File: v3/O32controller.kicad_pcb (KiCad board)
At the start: 4 copper layers, 27 x 27 mm, 88 parts, among them J1 SWD, J10 3V3, J11 GND, J12 I2C/RS485_2, J2 BATT+, J3 BATT-, J4 Motor Connection, J5 Motor Connection, J6 Motor Connection, J7 BATT+, J8 BATT-, J9 I2C/RS485_1, Q1 CSD88584Q5DCT, Q2 CSD88584Q5DCT, Q3 CSD88584Q5DCT, SW1 RESET, U1 MA702GQ-P, U2 STSPIN32F0A, U3 THVD1420DRLR

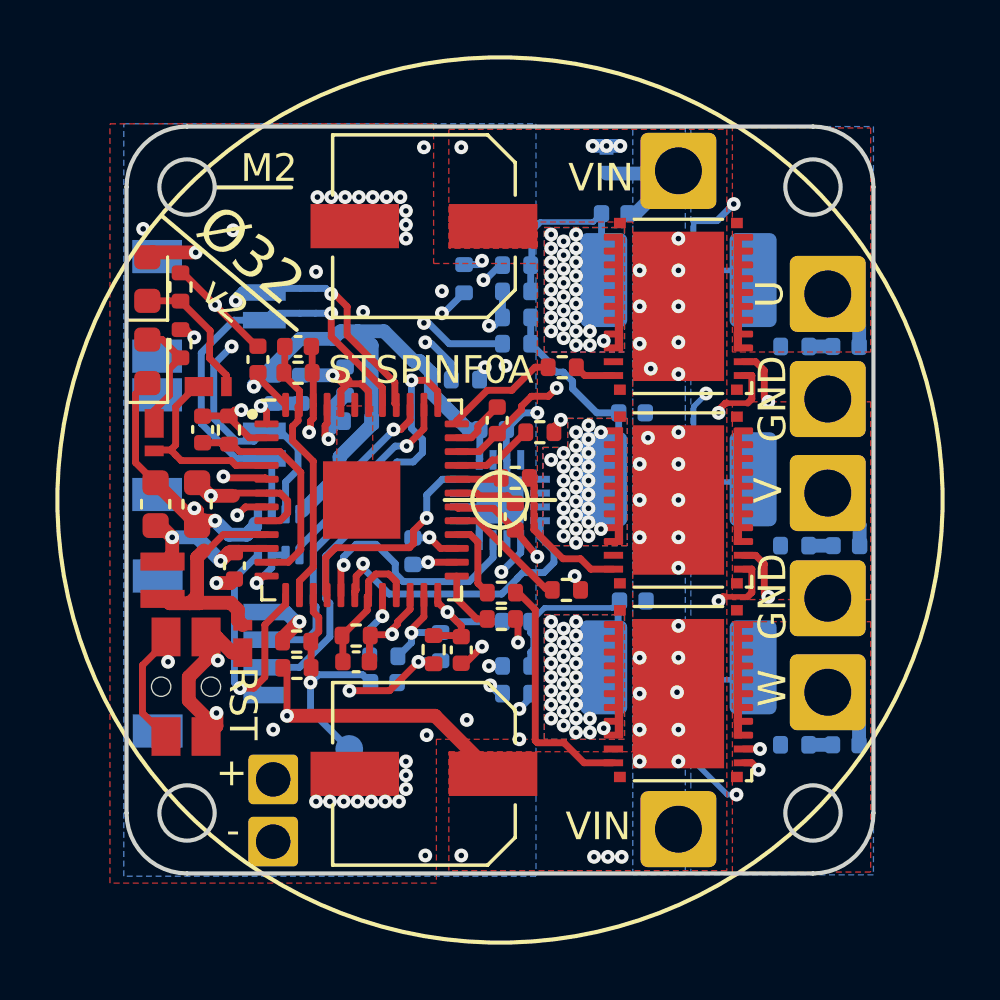
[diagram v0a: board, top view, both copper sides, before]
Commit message: external spi, update bus sns res, routing
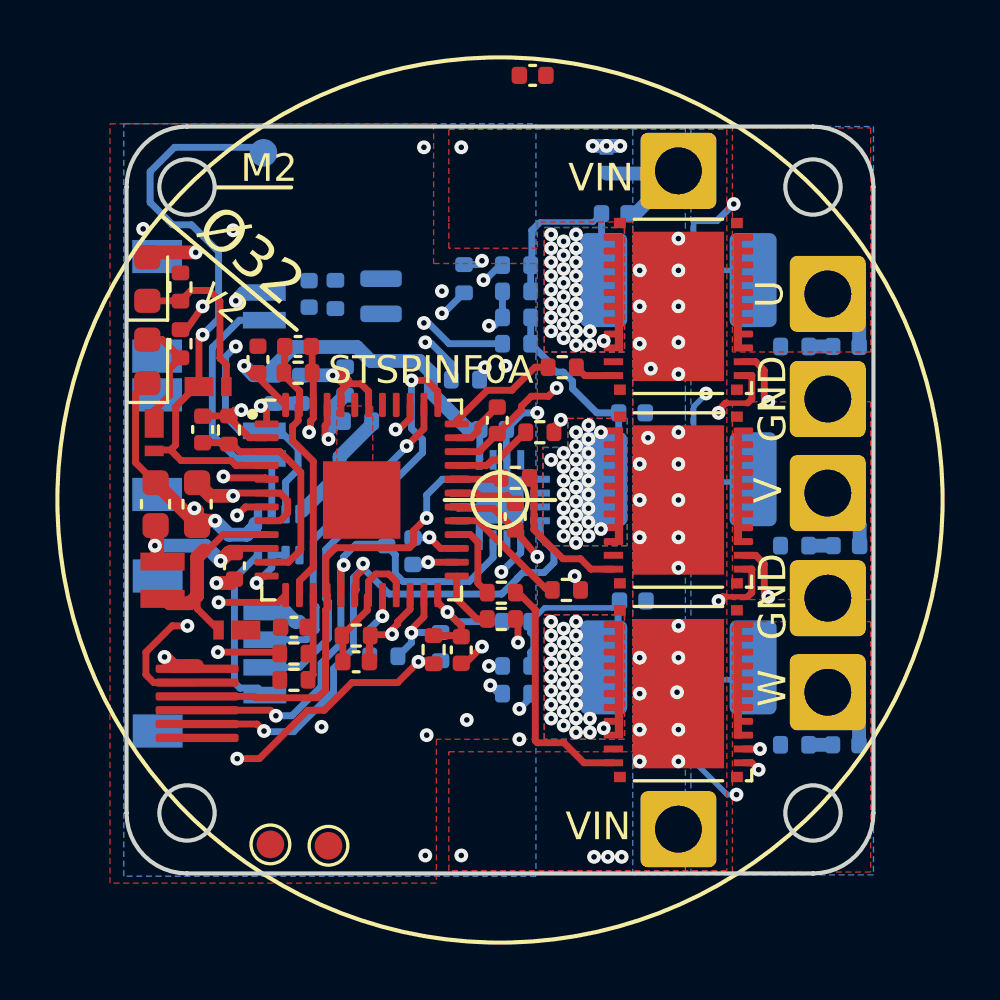
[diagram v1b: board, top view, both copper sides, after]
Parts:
- removed C21: 1nF, Capacitor_SMD:C_0402_1005Metric
- removed J10: 3V3, O32controller:SolderWire-Actual_1x01_D1.25mm_OD_1.8mm
- removed J11: GND, O32controller:SolderWire-Actual_1x01_D1.25mm_OD_1.8mm
- removed NT4: SDA/A, O32controller:NetTie-2_SMD_Pad0.25mm
- removed NT5: SCL/B, O32controller:NetTie-2_SMD_Pad0.25mm
- removed SW1: RESET, O32controller:Tactile_Switch_EVQ-P7A01P
- added C22: 100nF, Capacitor_SMD:C_0402_1005Metric, F.Cu at (42.5, 54.6)
- added J14: NTC, O32controller:SolderNTC-1.27mm, B.Cu at (45.7, 43.3)
- added J15: ExternalSPI, O32controller:FFC_0.5mm_6p, F.Cu at (39.0, 56.1)
- added R36: 1k, Resistor_SMD:R_0402_1005Metric, B.Cu at (44.0, 42.6)
- added R38: 13.7k, Resistor_SMD:R_0402_1005Metric, B.Cu at (45.9, 51.1)
- added TP1: TestPoint, TestPoint:TestPoint_Pad_D1.0mm, F.Cu at (43.8, 62.5)
- added TP2: TestPoint, TestPoint:TestPoint_Pad_D1.0mm, F.Cu at (41.7, 62.5)
- C8: value 100uF -> 20uF; footprint O32controller:CAP_EEEFN1E101UP -> Capacitor_SMD:C_0402_1005Metric
- C9: value 100uF -> 100nF; footprint O32controller:CAP_EEEFN1E101UP -> Capacitor_SMD:C_0402_1005Metric; moved to B.Cu
- J12: value I2C/RS485_2 -> RS485_2
- J9: value I2C/RS485_1 -> RS485_1
- R26: value 41.2k -> 54.9k
- R27: value 10k -> 13.7k
- moved TP3 21.8 mm to (41.5, 37.5)
- moved C9 17.8 mm to (43.1, 42.5), turned to -90 degrees
- moved C8 6.72 mm to (51.2, 34.6)
- moved R27 1.38 mm to (42.5, 56.5), turned to 0 degrees
- moved D1 0.54 mm to (40.5, 54.7), turned to 0 degrees
- moved R26 0.53 mm to (42.5, 55.5)
- renumbered TP2 to TP3
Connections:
- net /~{MAG_CS} renamed /~{MAG1_CS}
- C9 pad 1: VBUS -> /NTC_IN
- R27 pad 1: /BUS_SENSE -> GND
- R27 pad 2: GND -> /BUS_SENSE
- TP3 pad 1: /BUS_SENSE -> /LED_STATUS
- U2 pad 13: USART_TX -> /NTC_IN
- U2 pad 39: /USART_RX -> /~{MAG2_CS}
- U2 pad 40: I2C_SCL -> USART_TX
- U2 pad 41: I2C_SDA -> /USART_RX
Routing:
- net /NTC_IN: track 0.00 -> 22.8 mm, vias 0 -> 1
- net /~{MAG2_CS}: track 0.00 -> 20.3 mm, vias 0 -> 2
- net /LED_STATUS: track 6.93 -> 21.0 mm, vias 0 -> 1
- net GND: track 45.4 -> 33.8 mm, vias 51 -> 24
- net /SPI_MOSI: track 10.9 -> 21.6 mm, vias 1 -> 2
- net /SPI_MISO: track 8.81 -> 18.7 mm, vias 1 -> 2
- net /SPI_SCLK: track 8.16 -> 16.4 mm
- net /USART_RX: track 6.95 -> 0.00 mm, vias 1 -> 0
- net I2C_SCL: track 5.69 -> 0.00 mm, vias 1 -> 0
- net /BUS_SENSE: track 8.69 -> 3.14 mm, vias 1 -> 0
- net I2C_SDA: track 4.63 -> 0.00 mm, vias 1 -> 0
- net USART_TX: track 10.6 -> 6.25 mm, vias 1 -> 0
- net /RS485_B: track 13.4 -> 11.2 mm
- net /RS485_A: track 11.6 -> 9.80 mm
- net +3.3V: track 64.6 -> 62.8 mm, vias 7 -> 8
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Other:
- board text added: "A"
- board text added: "B"
- board text added: "NTC"
- board text removed: "+"
- board text removed: "-"
- board text removed: "3.3V"
- board text removed: "I2C,RS485"
- board text removed: "RST"
- board text removed: "SCL,B"
- board text removed: "SDA,A"
- board text removed: "SNS"

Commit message: bus caps, finished routing?
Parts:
- removed the TP1 at (43.8, 62.5)
- added C21: 22uF, O32controller:C_0805_nosilk, F.Cu at (42.4, 38.2)
- added C22: 22uF, O32controller:C_0805_nosilk, F.Cu at (44.4, 38.2)
- added C23: 22uF, O32controller:C_0805_nosilk, F.Cu at (46.3, 38.2)
- added C24: 22uF, O32controller:C_0805_nosilk, F.Cu at (48.3, 38.2)
- added C25: 22uF, O32controller:C_0805_nosilk, F.Cu at (50.3, 38.2)
- added C26: 22uF, O32controller:C_0805_nosilk, F.Cu at (52.2, 38.2)
- added C27: 22uF, O32controller:C_0805_nosilk, F.Cu at (42.4, 41.6)
- added C28: 22uF, O32controller:C_0805_nosilk, F.Cu at (44.4, 41.6)
- added C29: 22uF, O32controller:C_0805_nosilk, F.Cu at (46.3, 41.6)
- added C30: 22uF, O32controller:C_0805_nosilk, F.Cu at (48.3, 41.6)
- added C31: 22uF, O32controller:C_0805_nosilk, F.Cu at (50.5, 41.6)
- added C32: 22uF, O32controller:C_0805_nosilk, F.Cu at (42.5, 61.8)
- added C33: 22uF, O32controller:C_0805_nosilk, F.Cu at (44.5, 61.8)
- added C34: 22uF, O32controller:C_0805_nosilk, F.Cu at (46.5, 61.8)
- added C35: 22uF, O32controller:C_0805_nosilk, F.Cu at (48.5, 61.8)
- added C36: 22uF, O32controller:C_0805_nosilk, F.Cu at (50.4, 61.8)
- added C37: 22uF, O32controller:C_0805_nosilk, F.Cu at (52.4, 61.8)
- added C38: 22uF, O32controller:C_0805_nosilk, F.Cu at (49.5, 58.4)
- added C39: 22uF, O32controller:C_0805_nosilk, F.Cu at (47.5, 58.4)
- added C41: 22uF, O32controller:C_0805_nosilk, B.Cu at (52.6, 38.2)
- added C42: 22uF, O32controller:C_0805_nosilk, B.Cu at (50.7, 38.2)
- added C43: 22uF, O32controller:C_0805_nosilk, B.Cu at (48.7, 38.2)
- added C44: 22uF, O32controller:C_0805_nosilk, B.Cu at (46.7, 38.2)
- added C45: 22uF, O32controller:C_0805_nosilk, B.Cu at (44.8, 38.2)
- added C46: 22uF, O32controller:C_0805_nosilk, B.Cu at (42.8, 38.2)
- added C47: 22uF, O32controller:C_0805_nosilk, B.Cu at (46.5, 40.9)
- added C48: 22uF, O32controller:C_0805_nosilk, B.Cu at (43.1, 40.9)
- added C49: 22uF, O32controller:C_0805_nosilk, B.Cu at (53.5, 61.8)
- added C50: 22uF, O32controller:C_0805_nosilk, B.Cu at (51.5, 61.8)
- added C51: 22uF, O32controller:C_0805_nosilk, B.Cu at (49.5, 61.8)
- added C52: 22uF, O32controller:C_0805_nosilk, B.Cu at (47.5, 61.8)
- added C53: 22uF, O32controller:C_0805_nosilk, B.Cu at (45.5, 61.8)
- added C54: 22uF, O32controller:C_0805_nosilk, B.Cu at (43.5, 61.8)
- added C55: 22uF, O32controller:C_0805_nosilk, B.Cu at (49.9, 59.1)
- added C56: 22uF, O32controller:C_0805_nosilk, B.Cu at (47.1, 58.4)
- added C57: 22uF, O32controller:C_0805_nosilk, B.Cu at (45.1, 58.4)
- C40: renamed from C8; value 20uF -> 22uF; footprint Capacitor_SMD:C_0402_1005Metric -> O32controller:C_0805_nosilk
- TP1: renamed from TP3; footprint TestPoint:TestPoint_Pad_D1.0mm -> O32controller:TestPoint_Pad_Rect
- TP3: renamed from TP2; footprint TestPoint:TestPoint_Pad_D1.0mm -> O32controller:TestPoint_Pad_Rect; moved to B.Cu
- moved C40 24.4 mm to (45.5, 58.4), turned to 90 degrees
- moved R9 3.09 mm to (48.6, 52.5), turned to 0 degrees
- moved U2 2.20 mm to (43.4, 49.5), turned to 135 degrees
- moved J5 0.79 mm to (46.5, 43.2), turned to 90 degrees
- moved TP3 0.70 mm to (41.6, 61.8), turned to 180 degrees
- moved C9 0.66 mm to (43.0, 43.2), turned to 90 degrees
- moved R7 0.64 mm to (44.0, 43.2), turned to -90 degrees
- moved R32 0.54 mm to (44.5, 47.6), turned to -90 degrees
- moved C12 0.46 mm to (54.1, 39.2), turned to -90 degrees
- moved D2 0.36 mm to (54.1, 37.4)
- moved TP1 0.32 mm to (41.2, 37.7)
- moved L1 0.25 mm to (38.0, 52.9)
- moved R14 0.15 mm to (47.9, 55.5)
- moved R34 0.15 mm to (44.5, 45.7)
- moved C8 0.10 mm to (47.0, 51.9)
- renumbered C7 to C1, C22 to C10, C10 to C11, C18 to C14, C14 to C15, C15 to C16, C19 to C17, C16 to C18, C17 to C19, C1 to C6, C11 to C7, C6 to C8, D4 to D3, D5 to D4, D6 to D5, D3 to D6, J7 to J1, J4 to J10, J5 to J11, J6 to J12, J8 to J4, J14 to J5, J1 to J6, J15 to J7, J9 to J8, J12 to J9, R28 to R1, R27 to R10, R13 to R11, R23 to R12, R15 to R13, R30 to R14, R2 to R15, R31 to R16, R3 to R17, R1 to R18, R4 to R19, R29 to R2, R16 to R20, R24 to R21, R18 to R22, R32 to R23, R6 to R24, R33 to R25, R7 to R26, R5 to R27, R8 to R28, R19 to R29, R14 to R3, R25 to R30, R21 to R31, R34 to R32, R10 to R33, R35 to R34, R11 to R35, R9 to R36, R12 to R37, R22 to R4, R17 to R5, R20 to R6, R36 to R7, R26 to R8, R38 to R9, U2 to U1, U3 to U2, U1 to U3
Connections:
- J7 pad 1: +3.3V -> GND
- J7 pad 6: GND -> +3.3V
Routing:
- net USART_TX: track 6.25 -> 17.3 mm, vias 0 -> 1
- net GND: track 33.8 -> 40.9 mm, vias 24 -> 20
- net /LED_STATUS: track 21.0 -> 16.0 mm
- net /NRST: track 10.2 -> 14.8 mm
- net /USART_RX: track 0.00 -> 3.99 mm, vias 0 -> 1
- net /USART_DE: track 2.20 -> 5.52 mm
- net VBUS: track 28.5 -> 26.5 mm
- net /RS485_B: track 11.2 -> 9.75 mm
- net /OP_W_P: track 16.2 -> 16.9 mm
- net /SPI_MISO: track 18.7 -> 18.1 mm
- net /NTC_IN: track 22.8 -> 23.4 mm, vias 1 -> 2
- net /SPI_MOSI: track 21.6 -> 21.1 mm
- net +3.3V: track 62.8 -> 62.9 mm, vias 8 -> 7
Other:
- board text added: "+"
- board text added: "-"
- board text added: "10k"
- board text added: "7-15V"
- board text added: "D"
- board text added: "Ext.SPI"
- board text added: "JST-SH"
- board text added: "RST"
- board text added: "[12/27/23]"
- board text added: "v3"
- board text removed: "JST"
- board text removed: "SH"
- board text removed: "VIN: 7-15V"
- board text removed: "[1/6/23]"
- board text removed: "v2"

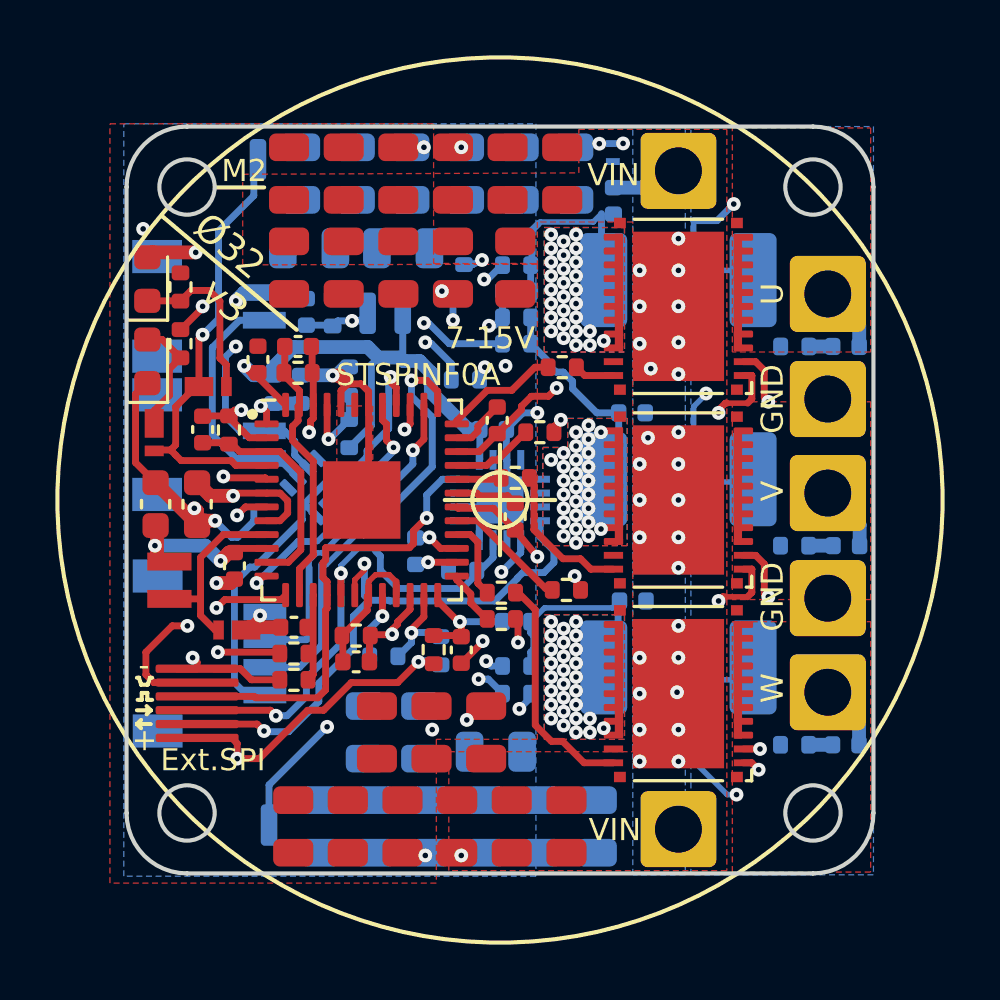
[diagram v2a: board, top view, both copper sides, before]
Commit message: add stitching vias, 0 drc errors
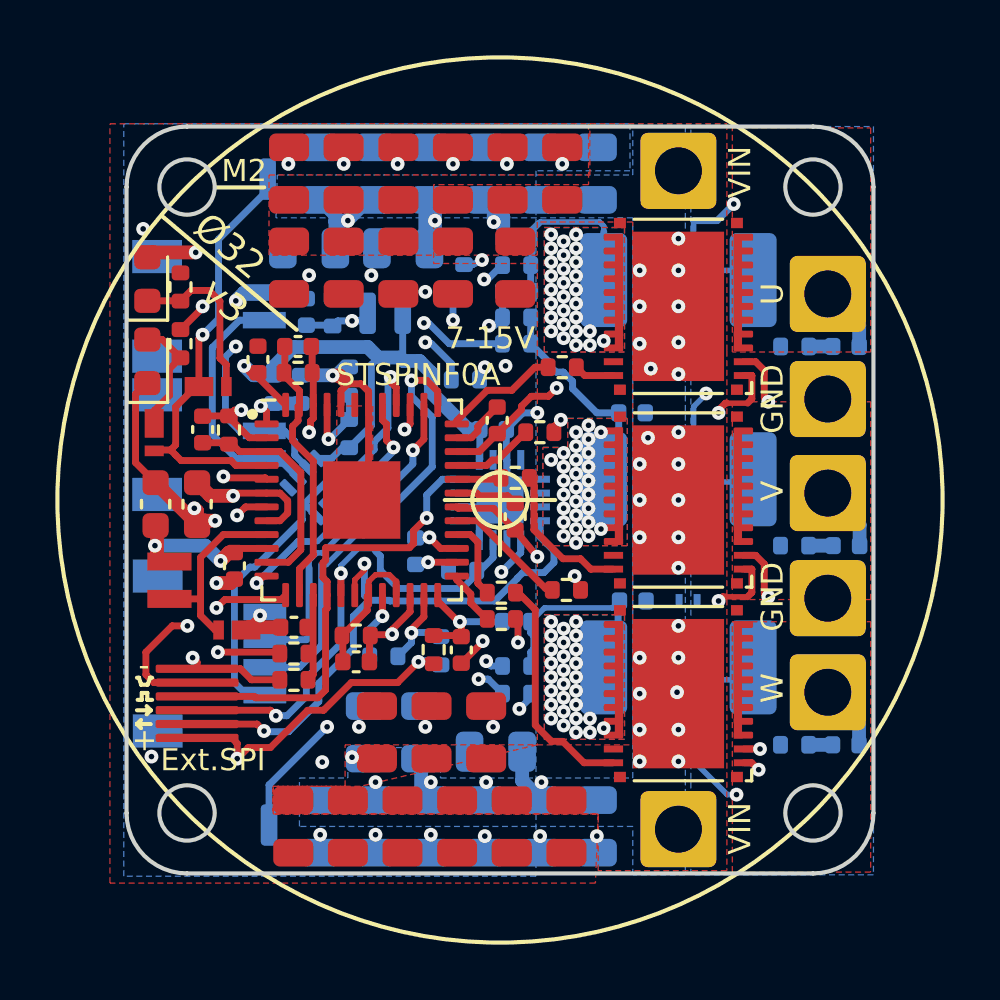
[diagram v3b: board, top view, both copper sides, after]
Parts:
- moved D2 16.4 mm to (56.8, 53.6), turned to 0 degrees
- moved C12 3.76 mm to (50.6, 40.5), turned to 0 degrees
- moved C41 0.85 mm to (53.5, 38.2)
- moved C42 0.83 mm to (51.5, 38.2)
- moved C43 0.80 mm to (49.5, 38.2)
- moved TP1 0.78 mm to (41.6, 38.4)
- moved C44 0.77 mm to (47.5, 38.2)
- moved C45 0.75 mm to (45.5, 38.2)
- moved C46 0.73 mm to (43.5, 38.2)
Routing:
- net VBUS: track 26.5 -> 41.9 mm, vias 29 -> 37
- net GND: track 40.9 -> 38.7 mm, vias 20 -> 31
- net +3.3V: track 62.9 -> 64.2 mm
- net /LED_STATUS: track 16.0 -> 15.5 mm
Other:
- board text added: "2mΩ 5W"
- board text removed: "locked"

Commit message: import pcbway cheapest capability drc rules
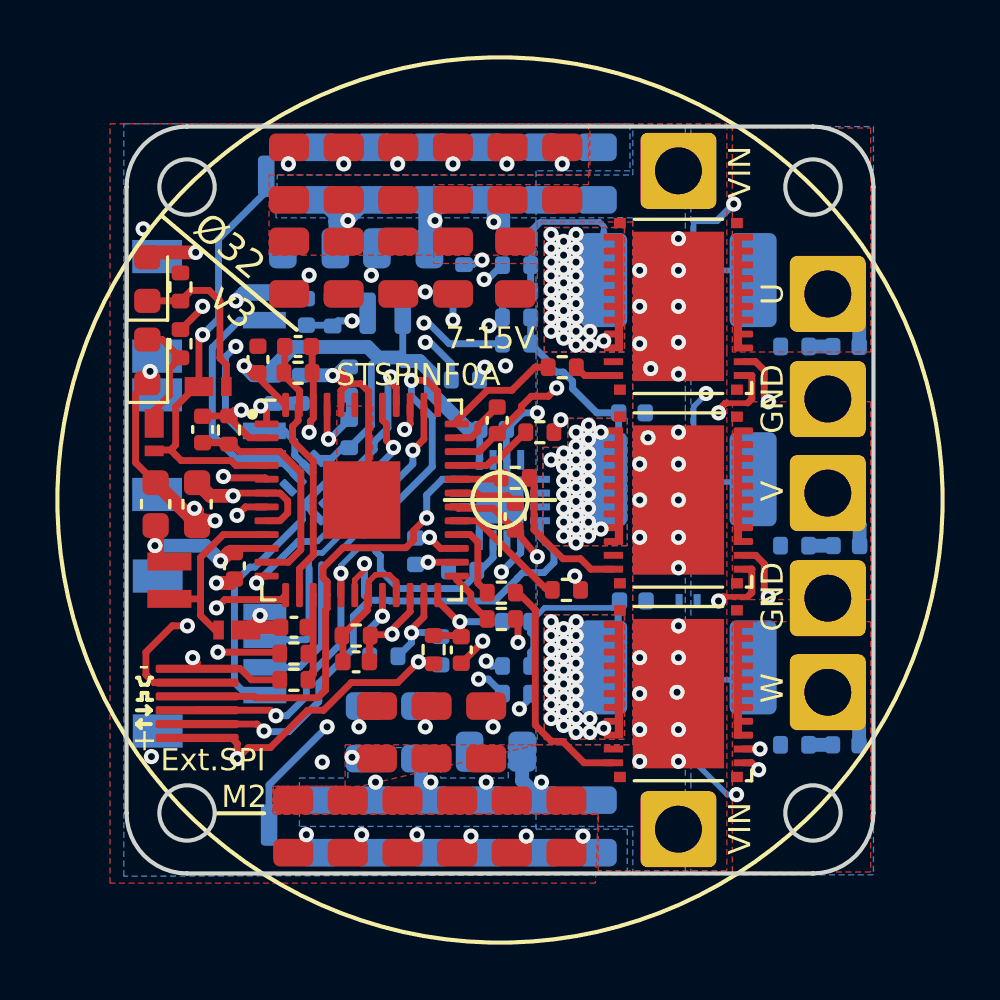
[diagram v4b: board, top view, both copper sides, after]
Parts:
- moved TP1 0.11 mm to (41.5, 38.3)
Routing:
- net GND: vias 31 -> 32
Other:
- board text added: "LED"
- board text added: "RS485"
- board text removed: "D"

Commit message: increase vias to 0.25 hole 0.55 dia
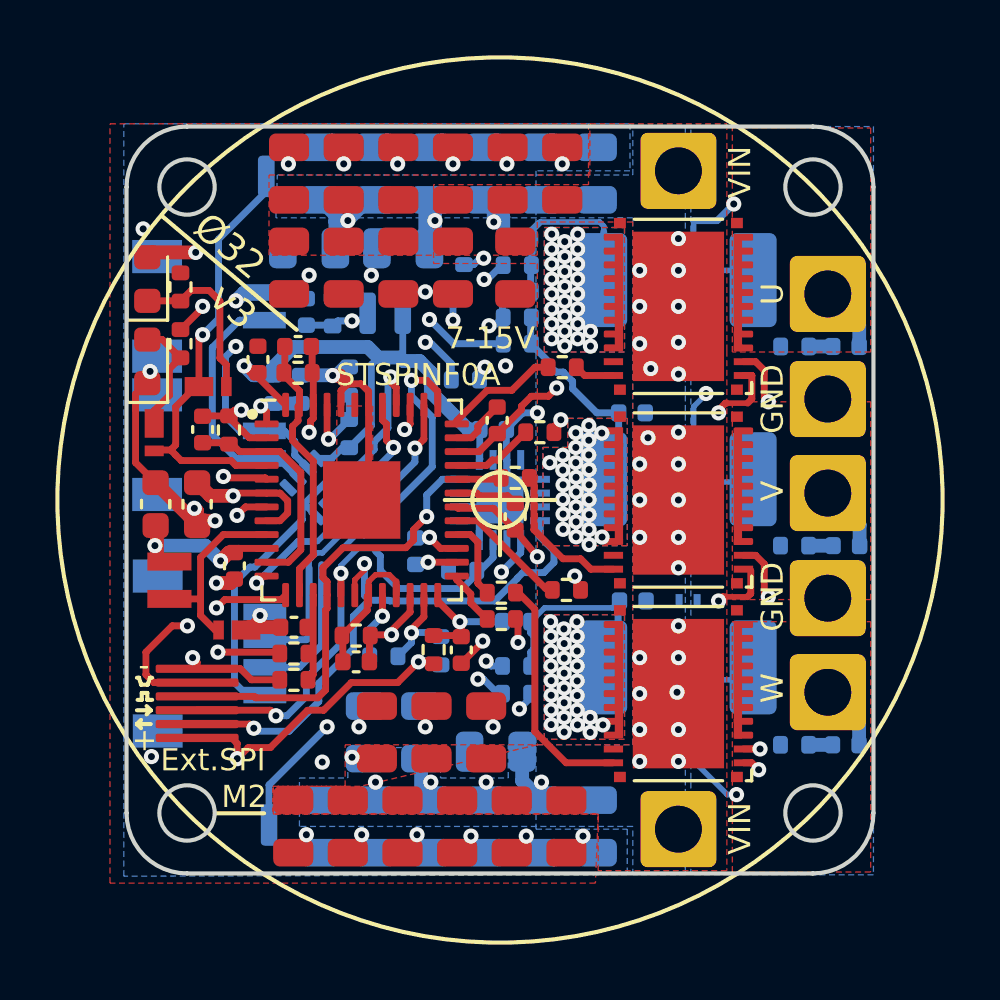
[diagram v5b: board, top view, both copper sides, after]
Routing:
- net /Motor phase W/SENSE_P: vias 28 -> 27
- net /Motor phase V/SENSE_P: vias 28 -> 26
- net /Motor phase U/SENSE_P: vias 28 -> 26

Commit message: export for PCBway
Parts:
- added C58: 100nF, Capacitor_SMD:C_0402_1005Metric, B.Cu at (41.7, 59.2)
- J8: value RS485_1 -> RS485
- J9: value RS485_2 -> RS485
- Q1, Q2, Q3: value CSD88584Q5DCT -> CSD88584Q5DC
- R18, R27, R36: value WSLF25122L000FEB 0.002R -> PU2512FKMP50R002L
- U1: value STSPIN32F0A -> STSPIN32F0ATR
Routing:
- net /Motor phase U/SENSE_P: vias 26 -> 27
